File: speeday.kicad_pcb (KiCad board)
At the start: 4 copper layers, 100 x 100 mm, 193 parts, among them IC1 Trig Cond Socket, IC2 LM3940IMP-3.3_NOPB, J1 Conn_01x04, J2 Micro_SD_Card, J3 Conn_01x04, J4 Conn_01x02, J5 Conn_02x20_Counter_Clockwise, J6 Screw_Terminal_01x02, P1 USB_C_Plug_USB2.0, Q1 SSM3K357R, Q2 SSM3K357R, Q3 SSM3K357R, SW1 SW_DIP_x01, SW2 SW_DIP_x01, SW3 SW_SPDT, U1 STM32F107V_B-C_Tx, U10 VNL5050, U11 MCP2551-I-SN, U12 VNL5050, U13 VNL5050, U14 VNL5050, U15 VNL5050, U16 IXDN602, U17 IXDN602, U18 LM2940S-5.0/NOPB, U2 TXB0108PW, U3 TXB0108PW, U4 W25Q16JVSS, U5 MPX4250, U6 SP720, U7 VNL5050, U8 VNL5050, U9 VNL5050, Y1 Crystal_GND23

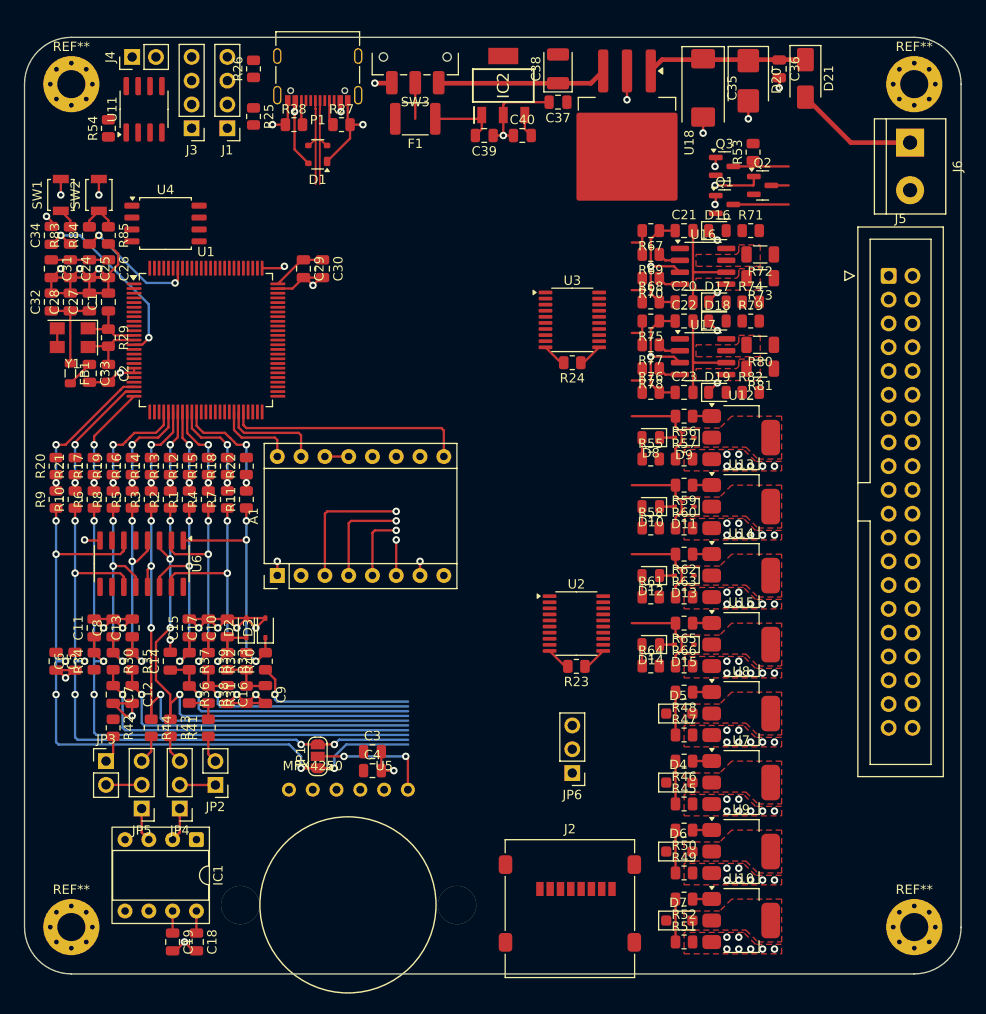
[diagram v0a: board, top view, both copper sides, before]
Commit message: Add additional IOs
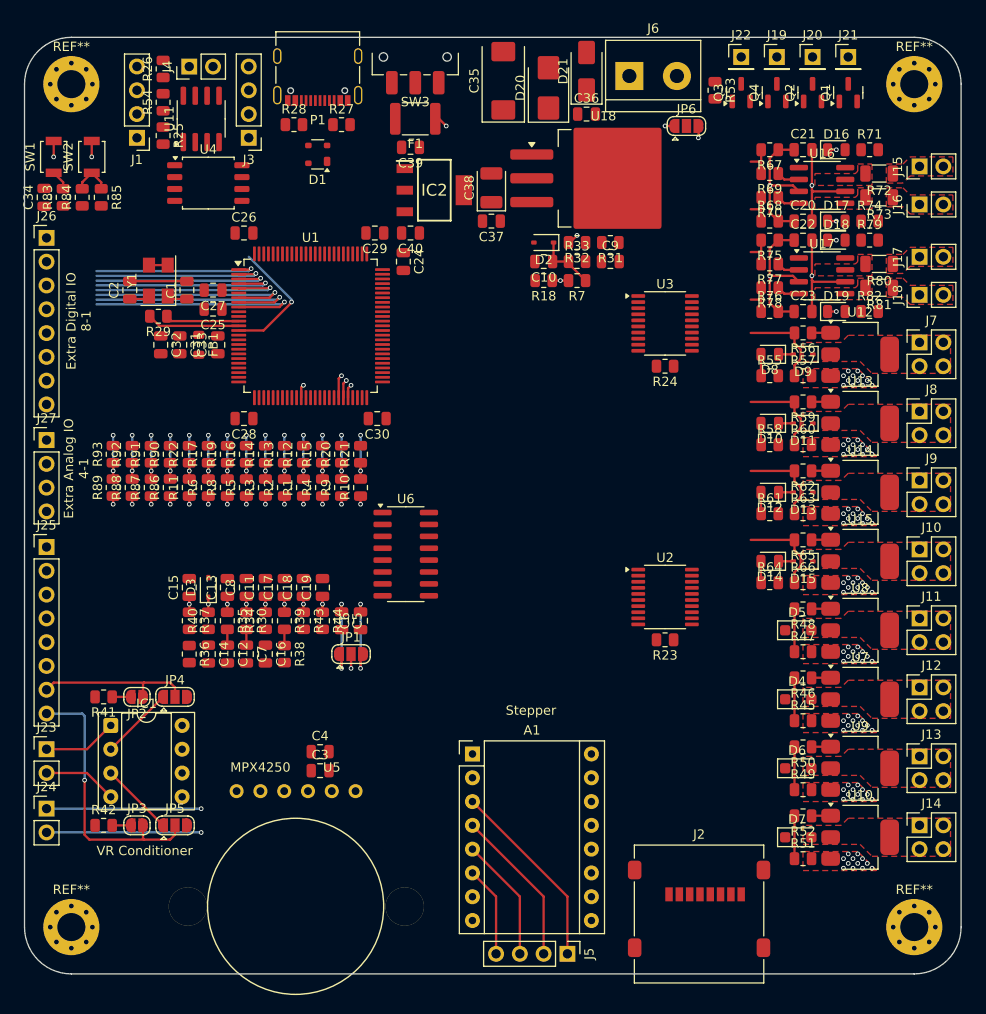
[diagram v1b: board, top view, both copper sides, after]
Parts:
- added J10: Conn_02x02_Counter_Clockwise, Connector_PinHeader_2.54mm:PinHeader_2x02_P2.54mm_Vertical, F.Cu at (115.6, 74.7)
- added J11: Conn_02x02_Counter_Clockwise, Connector_PinHeader_2.54mm:PinHeader_2x02_P2.54mm_Vertical, F.Cu at (115.6, 82.0)
- added J12: Conn_02x02_Counter_Clockwise, Connector_PinHeader_2.54mm:PinHeader_2x02_P2.54mm_Vertical, F.Cu at (115.6, 89.4)
- added J13: Conn_02x02_Counter_Clockwise, Connector_PinHeader_2.54mm:PinHeader_2x02_P2.54mm_Vertical, F.Cu at (115.6, 96.8)
- added J14: Conn_02x02_Counter_Clockwise, Connector_PinHeader_2.54mm:PinHeader_2x02_P2.54mm_Vertical, F.Cu at (115.6, 104.1)
- added J15: Conn_01x02, Connector_PinHeader_2.54mm:PinHeader_1x02_P2.54mm_Vertical, F.Cu at (115.6, 33.8)
- added J16: Conn_01x02, Connector_PinHeader_2.54mm:PinHeader_1x02_P2.54mm_Vertical, F.Cu at (115.6, 37.8)
- added J17: Conn_01x02, Connector_PinHeader_2.54mm:PinHeader_1x02_P2.54mm_Vertical, F.Cu at (115.6, 43.4)
- added J18: Conn_01x02, Connector_PinHeader_2.54mm:PinHeader_1x02_P2.54mm_Vertical, F.Cu at (115.6, 47.5)
- added J19: Conn_01x01, Connector_PinHeader_2.54mm:PinHeader_1x01_P2.54mm_Vertical, F.Cu at (100.3, 22.1)
- added J20: Conn_01x01, Connector_PinHeader_2.54mm:PinHeader_1x01_P2.54mm_Vertical, F.Cu at (104.1, 22.1)
- added J21: Conn_01x01, Connector_PinHeader_2.54mm:PinHeader_1x01_P2.54mm_Vertical, F.Cu at (108.0, 22.1)
- added J22: Conn_01x01, Connector_PinHeader_2.54mm:PinHeader_1x01_P2.54mm_Vertical, F.Cu at (96.5, 22.1)
- added J23: Conn_01x02, Connector_PinHeader_2.54mm:PinHeader_1x02_P2.54mm_Vertical, F.Cu at (22.4, 96.0)
- added J24: Conn_01x02, Connector_PinHeader_2.54mm:PinHeader_1x02_P2.54mm_Vertical, F.Cu at (22.4, 102.4)
- added J25: Conn_01x08, Connector_PinHeader_2.54mm:PinHeader_1x08_P2.54mm_Vertical, F.Cu at (22.4, 74.4)
- added J26: Conn_01x08, Connector_PinHeader_2.54mm:PinHeader_1x08_P2.54mm_Vertical, F.Cu at (22.4, 41.4)
- added J27: Conn_01x04, Connector_PinHeader_2.54mm:PinHeader_1x04_P2.54mm_Vertical, F.Cu at (22.4, 63.0)
- added J7: Conn_02x02_Counter_Clockwise, Connector_PinHeader_2.54mm:PinHeader_2x02_P2.54mm_Vertical, F.Cu at (115.6, 52.6)
- added J8: Conn_02x02_Counter_Clockwise, Connector_PinHeader_2.54mm:PinHeader_2x02_P2.54mm_Vertical, F.Cu at (115.6, 59.9)
- added J9: Conn_02x02_Counter_Clockwise, Connector_PinHeader_2.54mm:PinHeader_2x02_P2.54mm_Vertical, F.Cu at (115.6, 67.3)
- added Q4: SSM3K357R, Package_TO_SOT_SMD:SOT-23, F.Cu at (100.3, 25.9)
- added R86: 5k, Resistor_SMD:R_0805_2012Metric, F.Cu at (35.6, 68.1)
- added R87: 5k, Resistor_SMD:R_0805_2012Metric, F.Cu at (33.5, 68.1)
- added R88: 5k, Resistor_SMD:R_0805_2012Metric, F.Cu at (31.5, 68.1)
- added R89: 5k, Resistor_SMD:R_0805_2012Metric, F.Cu at (29.5, 68.1)
- added R90: 1k, Resistor_SMD:R_0805_2012Metric, F.Cu at (35.6, 64.5)
- added R91: 1k, Resistor_SMD:R_0805_2012Metric, F.Cu at (33.5, 64.5)
- added R92: 1k, Resistor_SMD:R_0805_2012Metric, F.Cu at (31.5, 64.5)
- added R93: 1k, Resistor_SMD:R_0805_2012Metric, F.Cu at (29.5, 64.5)
- J5: value Conn_02x20_Counter_Clockwise -> Conn_01x04; footprint Connector_IDC:IDC-Header_2x20_P2.54mm_Vertical -> Connector_PinHeader_2.54mm:PinHeader_1x04_P2.54mm_Vertical
- JP2, JP3: footprint Connector_PinHeader_2.54mm:PinHeader_1x02_P2.54mm_Vertical -> Jumper:SolderJumper-2_P1.3mm_Open_RoundedPad1.0x1.5mm
- JP4, JP5, JP6: footprint Connector_PinHeader_2.54mm:PinHeader_1x03_P2.54mm_Vertical -> Jumper:SolderJumper-3_P1.3mm_Open_RoundedPad1.0x1.5mm
- moved J5 80.1 mm to (78.0, 117.9), turned to -90 degrees
- moved JP6 70.2 mm to (90.7, 29.5), turned to 0 degrees
- moved R31 62.0 mm to (82.5, 41.9), turned to 180 degrees
- moved C9 59.1 mm to (82.5, 43.9), turned to 0 degrees
- moved R32 57.0 mm to (79.0, 41.9), turned to 180 degrees
- moved R33 56.7 mm to (79.0, 43.9), turned to 0 degrees
- moved D2 52.0 mm to (75.4, 41.9), turned to 180 degrees
- moved C10 51.7 mm to (75.4, 43.9), turned to 180 degrees
- moved R7 44.0 mm to (79.0, 46.0), turned to 180 degrees
- moved C19 41.1 mm to (51.8, 78.7), turned to 90 degrees
- moved C18 39.5 mm to (49.8, 78.7), turned to 90 degrees
- moved R18 39.2 mm to (75.4, 46.0), turned to 180 degrees
- moved C24 35.6 mm to (60.5, 43.9)
- moved J6 30.8 mm to (84.6, 24.1), turned to 0 degrees
- moved C6 30.8 mm to (55.9, 82.3)
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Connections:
- net MCU-UART-RX-EXTRA renamed MCU-UART-EXTRA-RX
- net MCU-UART-TX-EXTRA renamed MCU-UART-EXTRA-TX
- J5 pad 1: INJ-1-OUT -> STEP-A2
- J5 pad 2: INJ-1-OUT -> STEP-A1
- J5 pad 3: INJ-2-OUT -> STEP-B1
- J5 pad 4: INJ-2-OUT -> STEP-B2
- U1 pad 1: unconnected-(U1-PE2-Pad1) -> MCU-EXTRA-GPIO-1-D
- U1 pad 15: unconnected-(U1-PC0-Pad15) -> MCU-EXTRA-GPIO-9-A
- U1 pad 16: unconnected-(U1-PC1-Pad16) -> MCU-EXTRA-GPIO-10-A
- U1 pad 17: unconnected-(U1-PC2-Pad17) -> MCU-EXTRA-GPIO-11-A
- U1 pad 18: unconnected-(U1-PC3-Pad18) -> MCU-EXTRA-GPIO-12-A
- U1 pad 2: unconnected-(U1-PE3-Pad2) -> MCU-EXTRA-GPIO-2-D
- U1 pad 3: unconnected-(U1-PE4-Pad3) -> MCU-EXTRA-GPIO-3-D
- U1 pad 35: MCU-BAT-REF-IN-A -> MCU-CLUTCH-IN-A?
- U1 pad 36: MCU-CLUTCH-IN-A? -> MCU-BAT-REF-IN-A
- U1 pad 4: unconnected-(U1-PE5-Pad4) -> MCU-EXTRA-GPIO-4-D
- U1 pad 5: unconnected-(U1-PE6-Pad5) -> MCU-EXTRA-GPIO-5-D
- U1 pad 7: unconnected-(U1-PC13-Pad7) -> MCU-EXTRA-GPIO-6-D
- U1 pad 77: unconnected-(U1-PA15-Pad77) -> MCU-LC-TRIG-D
- U1 pad 78: MCU-UART-TX-BT -> MCU-UART-BT-TX
- U1 pad 79: MCU-UART-RX-BT -> MCU-UART-BT-RX
- U1 pad 8: unconnected-(U1-PC14-Pad8) -> MCU-EXTRA-GPIO-7-D
- U1 pad 9: unconnected-(U1-PC15-Pad9) -> MCU-EXTRA-GPIO-8-D
- U3 pad 1: MCU-TACHO-TRIG-D -> MCU-LC-TRIG-D
- U3 pad 16: unconnected-(U3-B4-Pad16) -> FAN-TRIG
- U3 pad 17: FAN-TRIG -> FUELPUMP-TRIG
- U3 pad 18: FUELPUMP-TRIG -> TACHO-TRIG
- U3 pad 20: TACHO-TRIG -> LC-TRIG
- U3 pad 3: MCU-FUELPUMP-TRIG-D -> MCU-TACHO-TRIG-D
- U3 pad 4: MCU-FAN-TRIG-D -> MCU-FUELPUMP-TRIG-D
- U3 pad 5: unconnected-(U3-A4-Pad5) -> MCU-FAN-TRIG-D
- U6 pad 1: RAW-CLUTCH -> unconnected-(U6-I1-Pad1)
- U6 pad 11: RAW-BARO-IN -> unconnected-(U6-I10-Pad11)
- U6 pad 12: RAW-O2 -> unconnected-(U6-I11-Pad12)
- U6 pad 13: RAW-CAM-IN -> unconnected-(U6-I12-Pad13)
- U6 pad 14: RAW-IAT -> unconnected-(U6-I13-Pad14)
- U6 pad 15: RAW-BAT-REF -> unconnected-(U6-I14-Pad15)
- U6 pad 2: RAW-COOLANT -> unconnected-(U6-I2-Pad2)
- U6 pad 3: RAW-CRANK-IN -> unconnected-(U6-I3-Pad3)
- U6 pad 4: RAW-TPS -> unconnected-(U6-I4-Pad4)
- U6 pad 5: RAW-FLEX -> unconnected-(U6-I5-Pad5)
- U6 pad 6: RAW-MAP-IN -> unconnected-(U6-I6-Pad6)
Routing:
- net GND: track 187.6 -> 43.9 mm, vias 92 -> 103
- net RAW-FLEX-IN: track 61.7 -> 2.56 mm, vias 3 -> 2
- net RAW-CAM-IN: track 59.4 -> 2.56 mm, vias 4 -> 2
- net RAW-CRANK-IN: track 58.2 -> 2.56 mm, vias 4 -> 2
- net RAW-MAP-IN: track 75.8 -> 26.7 mm, vias 6 -> 4
- net RAW-BARO-IN: track 68.1 -> 26.7 mm, vias 6 -> 4
- net O2-IN: track 37.2 -> 1.69 mm, vias 1 -> 0
- net TPS-IN: track 34.7 -> 1.69 mm, vias 1 -> 0
- net IAT-IN: track 29.2 -> 0.00 mm, vias 1 -> 0
- net CAM-IN: track 3.81 -> 29.5 mm, vias 0 -> 1
- net MCU-EXTRA-GPIO-8-D: track 0.00 -> 25.3 mm, vias 0 -> 1
- net COOLANT-IN: track 26.6 -> 1.73 mm, vias 1 -> 0
- net MCU-STEPPER-EN-D: track 25.8 -> 1.46 mm, vias 0 -> 1
- net MCU-EXTRA-GPIO-7-D: track 0.00 -> 24.3 mm, vias 0 -> 1
- net +3.3V: track 25.9 -> 1.70 mm
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- added copper zone on F.Cu, net IGN-1-OUT
- added copper zone on F.Cu, net IGN-2-OUT
- added copper zone on F.Cu, net IGN-3-OUT
- added copper zone on F.Cu, net IGN-4-OUT
- removed copper zone on In2.Cu, net +3.3V
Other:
- board text added: "Extra Analog IO 4-1"
- board text added: "Extra Digital IO 8-1"
- board text added: "Stepper"
- board text added: "VR Conditioner"

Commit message: Pre MCU switch
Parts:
- removed U10, U12, U13, U14, U15, U7, U8, U9: VNL5050, IC_Automotive:SOT-223-3_VNL5050
- added D22: D, Diode_SMD:D_SOD-323, F.Cu at (99.6, 90.7)
- added D23: LED, LED_SMD:LED_0805_2012Metric, F.Cu at (96.0, 90.7)
- added D24: D, Diode_SMD:D_SOD-323, F.Cu at (99.6, 83.3)
- added D25: LED, LED_SMD:LED_0805_2012Metric, F.Cu at (96.0, 83.3)
- added D26: D, Diode_SMD:D_SOD-323, F.Cu at (99.6, 98.0)
- added D27: LED, LED_SMD:LED_0805_2012Metric, F.Cu at (96.0, 98.0)
- added D28: D, Diode_SMD:D_SOD-323, F.Cu at (99.6, 105.4)
- added D29: LED, LED_SMD:LED_0805_2012Metric, F.Cu at (96.0, 105.4)
- added IC10: VNL5090N3-E, IC_Automotive:SOT230P700X180-4N, F.Cu at (109.5, 75.9)
- added IC3: VNL5090N3-E, IC_Automotive:SOT230P700X180-4N, F.Cu at (109.5, 90.7)
- added IC4: VNL5090N3-E, IC_Automotive:SOT230P700X180-4N, F.Cu at (109.5, 83.3)
- added IC5: VNL5090N3-E, IC_Automotive:SOT230P700X180-4N, F.Cu at (109.5, 98.0)
- added IC6: VNL5090N3-E, IC_Automotive:SOT230P700X180-4N, F.Cu at (109.5, 105.4)
- added IC7: VNL5090N3-E, IC_Automotive:SOT230P700X180-4N, F.Cu at (109.5, 53.8)
- added IC8: VNL5090N3-E, IC_Automotive:SOT230P700X180-4N, F.Cu at (109.5, 61.2)
- added IC9: VNL5090N3-E, IC_Automotive:SOT230P700X180-4N, F.Cu at (109.5, 68.6)
- added R94: 2.4k, Resistor_SMD:R_0805_2012Metric, F.Cu at (96.0, 88.4)
- added R95: 2.4k, Resistor_SMD:R_0805_2012Metric, F.Cu at (96.0, 81.0)
- added R96: 2.4k, Resistor_SMD:R_0805_2012Metric, F.Cu at (96.0, 95.8)
- added R97: 2.4k, Resistor_SMD:R_0805_2012Metric, F.Cu at (96.0, 103.1)
- D10, D12, D14: value LED -> D; footprint LED_SMD:LED_0805_2012Metric -> Diode_SMD:D_SOD-323
- D11, D13, D15: value D -> LED; footprint Diode_SMD:D_SOD-323 -> LED_SMD:LED_0805_2012Metric
- D4, D5, D6, D7: footprint Diode_SMD:D_SOD-123F -> Diode_SMD:D_SOD-323
- R47, R49, R51: value 100k -> 1k
- R48, R50, R52, R59, R62, R65: value 1k -> 100k
- R58, R61, R64: value 2.4k -> 1k
- R60, R63, R66: value 100k -> 2.4k
- moved A1 14.0 mm to (61.5, 84.1)
- moved R1 12.2 mm to (37.6, 68.1)
- moved R12 12.2 mm to (37.6, 64.5)
- moved D16 11.0 mm to (96.0, 34.5)
- moved R71 11.0 mm to (99.6, 34.5)
- moved R60 8.45 mm to (96.0, 58.9), turned to 180 degrees
- moved R63 8.45 mm to (96.0, 66.3), turned to 180 degrees
- moved R66 8.45 mm to (96.0, 73.7), turned to 180 degrees
- moved J2 8.06 mm to (84.0, 114.1)
- moved D11 7.11 mm to (96.0, 61.2)
- moved D13 7.11 mm to (96.0, 68.6)
- moved D15 7.11 mm to (96.0, 75.9)
- moved J5 6.36 mm to (71.6, 118.1)
- moved R14 6.10 mm to (51.8, 64.5)
- moved R3 6.10 mm to (51.8, 68.1)
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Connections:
- D10 pad 1: Net-(D10-K) -> INJ-2-OUT
- D11 pad 1: INJ-2-OUT -> Net-(D10-A)
- D11 pad 2: Net-(D10-K) -> Net-(D11-A)
- D12 pad 1: Net-(D12-K) -> INJ-3-OUT
- D13 pad 1: INJ-3-OUT -> Net-(D12-A)
- D13 pad 2: Net-(D12-K) -> Net-(D13-A)
- D14 pad 1: Net-(D14-K) -> INJ-4-OUT
- D15 pad 1: INJ-4-OUT -> Net-(D14-A)
- D15 pad 2: Net-(D14-K) -> Net-(D15-A)
- J25 pad 1: O2-IN -> RAW-FLEX-IN
- J25 pad 2: TPS-IN -> IAT-IN
- J25 pad 3: IAT-IN -> CLUTCH-IN
- J25 pad 4: RAW-FLEX-IN -> TPS-IN
- J25 pad 5: COOLANT-IN -> O2-IN
- J25 pad 6: CLUTCH-IN -> COOLANT-IN
- J26 pad 1: EXTRA-GPIO-1-D -> MCU-EXTRA-GPIO-1-D
- J26 pad 2: EXTRA-GPIO-2-D -> MCU-EXTRA-GPIO-2-D
- J26 pad 3: EXTRA-GPIO-3-D -> MCU-EXTRA-GPIO-3-D
- J26 pad 4: EXTRA-GPIO-4-D -> MCU-EXTRA-GPIO-4-D
- J26 pad 5: EXTRA-GPIO-5-D -> MCU-EXTRA-GPIO-5-D
- J26 pad 6: EXTRA-GPIO-6-D -> MCU-EXTRA-GPIO-6-D
- J26 pad 7: EXTRA-GPIO-7-D -> MCU-EXTRA-GPIO-7-D
- J26 pad 8: EXTRA-GPIO-8-D -> MCU-EXTRA-GPIO-8-D
- J3 pad 1: MCU-UART-TX-BT -> MCU-UART-BT-TX
- J3 pad 2: MCU-UART-RX-BT -> MCU-UART-BT-RX
- J6 pad 1: +12V -> RAW-BAT
- JP6 pad 3: +12V -> RAW-BAT
- R47 pad 1: IDLE-TRIG -> Net-(IC4-INPUT)
- R47 pad 2: GND -> IDLE-TRIG
- R48 pad 1: Net-(U8-IN) -> IDLE-TRIG
- R48 pad 2: IDLE-TRIG -> GND
- R49 pad 1: HC1-TRIG -> Net-(IC5-INPUT)
- R49 pad 2: GND -> HC1-TRIG
- R50 pad 1: Net-(U9-IN) -> HC1-TRIG
- R50 pad 2: HC1-TRIG -> GND
- R51 pad 1: HC2-TRIG -> Net-(IC6-INPUT)
- R51 pad 2: GND -> HC2-TRIG
- R52 pad 1: Net-(U10-IN) -> HC2-TRIG
- R52 pad 2: HC2-TRIG -> GND
- R55 pad 1: Net-(D8-A) -> +12V
- R55 pad 2: +12V -> Net-(D8-A)
- R57 pad 1: INJ-1-TRIG -> GND
- R57 pad 2: GND -> INJ-1-TRIG
- R58 pad 1: Net-(D10-A) -> Net-(IC8-INPUT)
- R58 pad 2: +12V -> INJ-2-TRIG
- R59 pad 1: Net-(U13-IN) -> GND
- R60 pad 1: INJ-2-TRIG -> +12V
- R60 pad 2: GND -> Net-(D11-A)
- R61 pad 1: Net-(D12-A) -> Net-(IC9-INPUT)
- R61 pad 2: +12V -> INJ-3-TRIG
- R62 pad 1: Net-(U14-IN) -> GND
- R63 pad 1: INJ-3-TRIG -> +12V
- R63 pad 2: GND -> Net-(D13-A)
- R64 pad 1: Net-(D14-A) -> Net-(IC10-INPUT)
- R64 pad 2: +12V -> INJ-4-TRIG
- R65 pad 1: Net-(U15-IN) -> GND
- R66 pad 1: INJ-4-TRIG -> +12V
- R66 pad 2: GND -> Net-(D15-A)
- R7 pad 1: RAW-BAT-REF -> RAW-BAT
- U1 pad 23: MCU-MAP-IN-A -> MCU-IAT-IN-A
- U1 pad 24: MCU-BARO-IN-A -> MCU-CLUTCH-IN-A?
- U1 pad 25: MCU-FLEX-IN-A -> MCU-TPS-IN-A
- U1 pad 30: MCU-TPS-IN-A -> MCU-FLEX-IN-A
- U1 pad 31: MCU-CAM-IN-A -> MCU-CLT-IN-A
- U1 pad 33: MCU-IAT-IN-A -> MCU-CAM-IN-A
- U1 pad 34: MCU-CLT-IN-A -> MCU-MAP-IN-A
- U1 pad 35: MCU-CLUTCH-IN-A? -> MCU-BARO-IN-A
- U1 pad 59: MCU-IGN-1-TRIG-D -> MCU-INJ-4-TRIG-D
- U1 pad 60: MCU-IGN-2-TRIG-D -> MCU-INJ-3-TRIG-D
- U1 pad 61: MCU-IGN-3-TRIG-D -> MCU-INJ-2-TRIG-D
- U1 pad 62: MCU-IGN-4-TRIG-D -> MCU-INJ-1-TRIG-D
- U1 pad 63: MCU-INJ-4-TRIG-D -> MCU-IGN-4-TRIG-D
- U1 pad 64: MCU-INJ-3-TRIG-D -> MCU-IGN-3-TRIG-D
- U1 pad 65: MCU-INJ-2-TRIG-D -> MCU-IGN-2-TRIG-D
- U1 pad 66: MCU-INJ-1-TRIG-D -> MCU-IGN-1-TRIG-D
- U3 pad 6: MCU-IGN-4-TRIG-D -> MCU-IGN-1-TRIG-D
- U3 pad 7: MCU-IGN-3-TRIG-D -> MCU-IGN-2-TRIG-D
- U3 pad 8: MCU-IGN-2-TRIG-D -> MCU-IGN-3-TRIG-D
- U3 pad 9: MCU-IGN-1-TRIG-D -> MCU-IGN-4-TRIG-D
- U6 pad 1: unconnected-(U6-I1-Pad1) -> RAW-O2
- U6 pad 10: unconnected-(U6-I9-Pad10) -> RAW-CLUTCH
- U6 pad 11: unconnected-(U6-I10-Pad11) -> RAW-IAT
- U6 pad 12: unconnected-(U6-I11-Pad12) -> RAW-EXTRA-GPIO-9-A
- U6 pad 13: unconnected-(U6-I12-Pad13) -> RAW-EXTRA-GPIO-10-A
- U6 pad 14: unconnected-(U6-I13-Pad14) -> RAW-EXTRA-GPIO-11-A
- U6 pad 15: unconnected-(U6-I14-Pad15) -> RAW-EXTRA-GPIO-12-A
- U6 pad 2: unconnected-(U6-I2-Pad2) -> RAW-FLEX-IN
- U6 pad 3: unconnected-(U6-I3-Pad3) -> RAW-COOLANT
- U6 pad 4: unconnected-(U6-I4-Pad4) -> RAW-CRANK-IN
- U6 pad 5: unconnected-(U6-I5-Pad5) -> RAW-CAM-IN
- U6 pad 6: unconnected-(U6-I6-Pad6) -> RAW-MAP-IN
- U6 pad 7: unconnected-(U6-I7-Pad7) -> RAW-BARO-IN
- U6 pad 9: unconnected-(U6-I8-Pad9) -> RAW-TPS
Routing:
- net MCU-SPI-SD-MISO: track 0.00 -> 80.2 mm, vias 0 -> 1
- net MCU-SPI-SD-CLK: track 0.00 -> 77.8 mm, vias 0 -> 1
- net MCU-SPI-SD-MOSI: track 0.00 -> 77.2 mm, vias 0 -> 2
- net MCU-SD-CS-OUT-D: track 0.00 -> 74.3 mm, vias 0 -> 1
- net MCU-STEPPER-EN-D: track 1.46 -> 62.2 mm, vias 1 -> 2
- net RAW-FLEX-IN: track 2.56 -> 56.8 mm, vias 2 -> 6
- net MCU-HC-2-TRIG-D: track 0.00 -> 53.2 mm
- net MCU-HC-1-TRIG-D: track 0.00 -> 53.0 mm
- net MCU-BOOST-TRIG-D: track 0.00 -> 52.7 mm
- net MCU-IDLE-TRIG-D: track 0.00 -> 52.5 mm
- net MCU-INJ-4-TRIG-D: track 0.00 -> 52.3 mm
- net MCU-INJ-3-TRIG-D: track 0.00 -> 52.1 mm
- net MCU-INJ-2-TRIG-D: track 0.00 -> 51.9 mm
- net MCU-INJ-1-TRIG-D: track 0.00 -> 51.4 mm
- net MCU-STEPPER-STEP-D: track 1.96 -> 49.7 mm, vias 1 -> 2
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
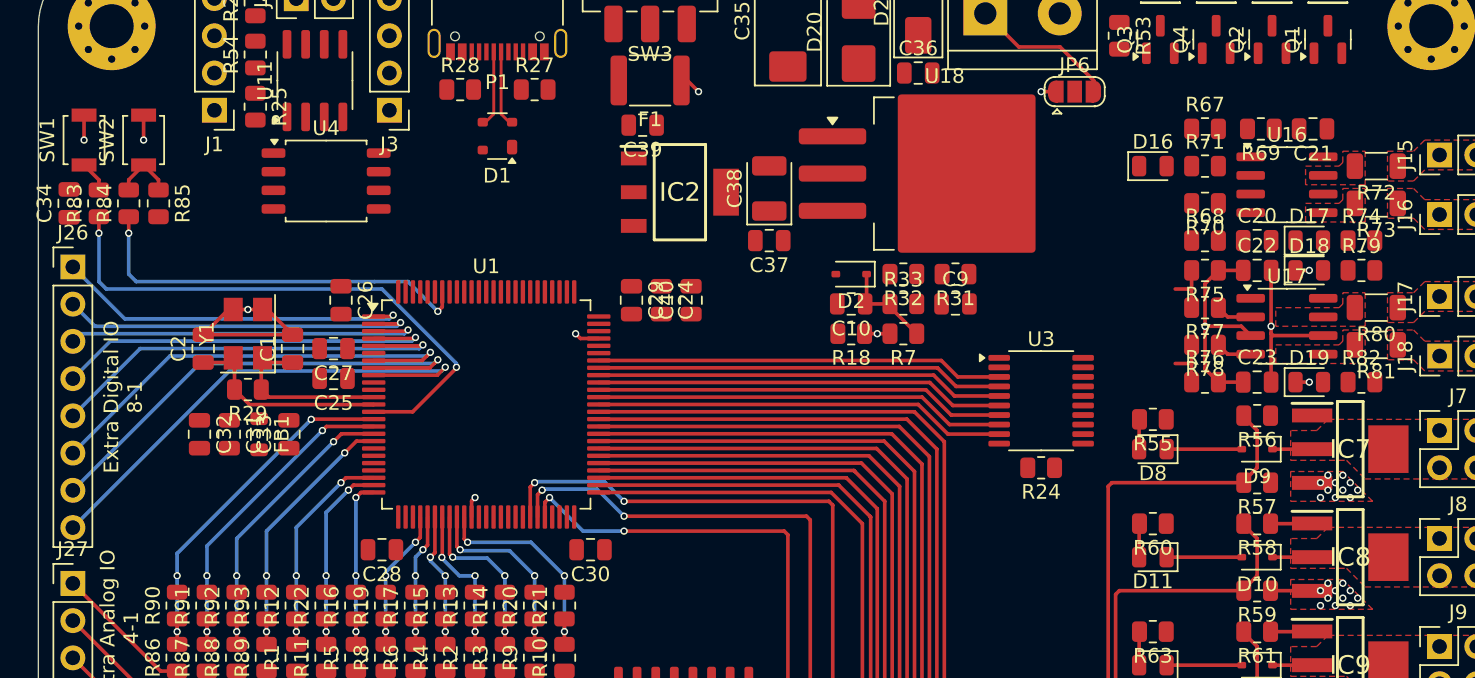
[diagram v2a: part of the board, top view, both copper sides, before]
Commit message: Fix MCU decoupling capacitors
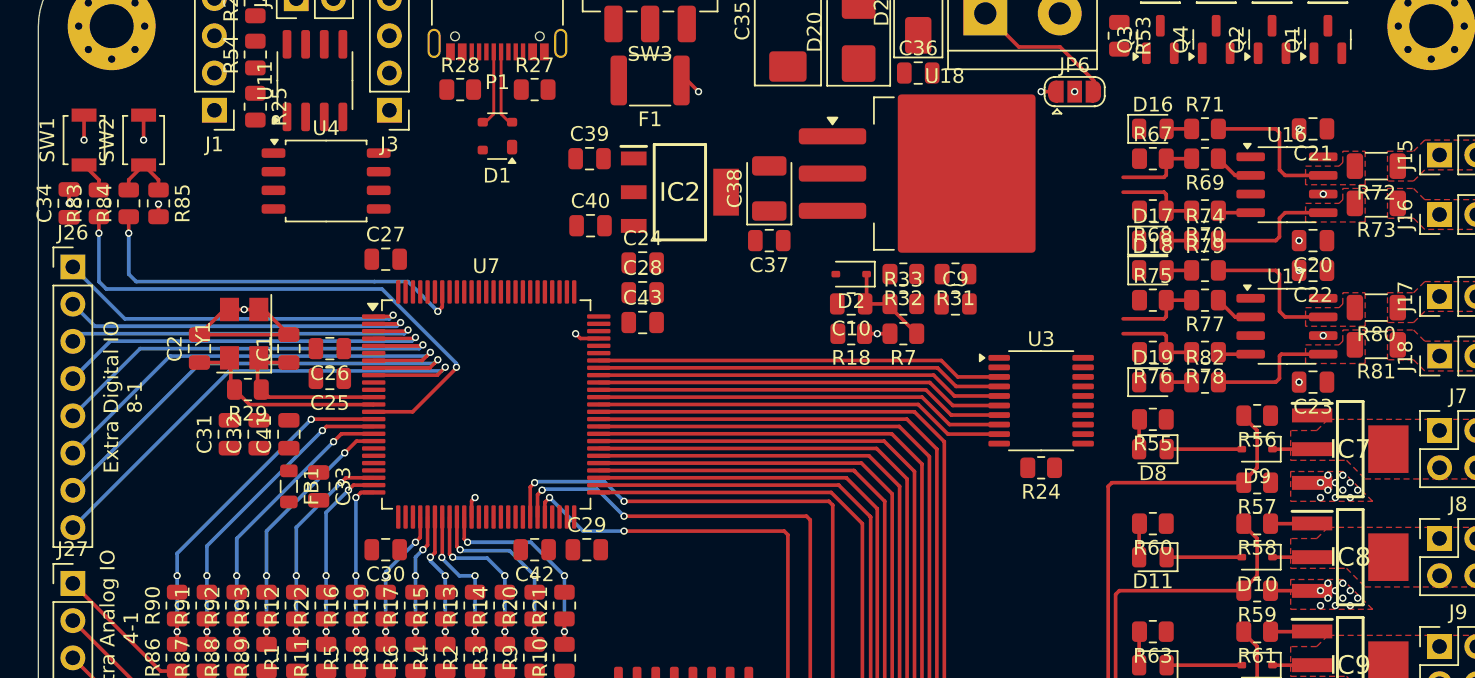
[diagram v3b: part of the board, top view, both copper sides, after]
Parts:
- removed U1: STM32F107V_B-C_Tx, Package_QFP:LQFP-100_14x14mm_P0.5mm
- added C41: 100n, Capacitor_SMD:C_0805_2012Metric, F.Cu at (37.1, 52.8)
- added C42: 2.2µ, Capacitor_SMD:C_0805_2012Metric, F.Cu at (53.8, 60.7)
- added C43: 2.2µ, Capacitor_SMD:C_0805_2012Metric, F.Cu at (61.2, 45.2)
- added U7: STM32F407VGTx, Package_QFP:LQFP-100_14x14mm_P0.5mm, F.Cu at (50.5, 50.8)
- moved C28 25.0 mm to (61.2, 43.2), turned to 0 degrees
- moved C29 17.3 mm to (57.4, 60.7), turned to 0 degrees
- moved C30 14.0 mm to (43.7, 60.7)
- moved D17 10.7 mm to (96.0, 39.6)
- moved D18 10.7 mm to (96.0, 41.7)
- moved D19 10.7 mm to (96.0, 49.3)
- moved R74 10.7 mm to (99.6, 39.6)
- moved R79 10.7 mm to (99.6, 41.7)
- moved R82 10.7 mm to (99.6, 49.3)
- moved C40 8.53 mm to (57.7, 38.6), turned to 0 degrees
- moved C27 7.06 mm to (43.7, 40.9), turned to 0 degrees
- moved R69 4.32 mm to (99.6, 34.0)
- moved C39 4.28 mm to (57.6, 34.0), turned to 0 degrees
- moved FB1 4.10 mm to (37.1, 56.4)
- moved R67 4.10 mm to (96.0, 34.0)
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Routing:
- net GND: track 52.3 -> 37.0 mm, vias 93 -> 92
- net Vdrive: track 11.2 -> 0.00 mm, vias 1 -> 7
- net Net-(U17-OUT_A): track 0.00 -> 9.95 mm
- net Net-(U16-OUT_A): track 0.00 -> 9.95 mm
- net Net-(U17-OUT_B): track 0.00 -> 8.83 mm
- net Net-(U16-OUT_B): track 0.00 -> 8.68 mm
- net IGN-2-TRIG: track 0.00 -> 5.86 mm
- net IGN-1-TRIG: track 0.00 -> 5.86 mm
- net Net-(U16-IN_A): track 0.00 -> 2.67 mm
- net Net-(U16-IN_B): track 0.00 -> 2.25 mm
- net IGN-4-TRIG: track 3.66 -> 5.86 mm
- net IGN-3-TRIG: track 3.66 -> 5.86 mm
- net Net-(D19-A): track 0.00 -> 1.71 mm
- net Net-(D18-A): track 0.00 -> 1.71 mm
- net Net-(D17-A): track 0.00 -> 1.71 mm
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- added copper zone on In2.Cu, net Vdrive
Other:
- board text added: "...VCAP"
- board text added: "VCAP..."
